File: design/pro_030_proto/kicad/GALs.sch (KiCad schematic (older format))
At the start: 11 parts, among them IC10 ATF22V10C, IC11 ATF22V10C, IC12 ATF22V10C, IC9 ATF22V10C

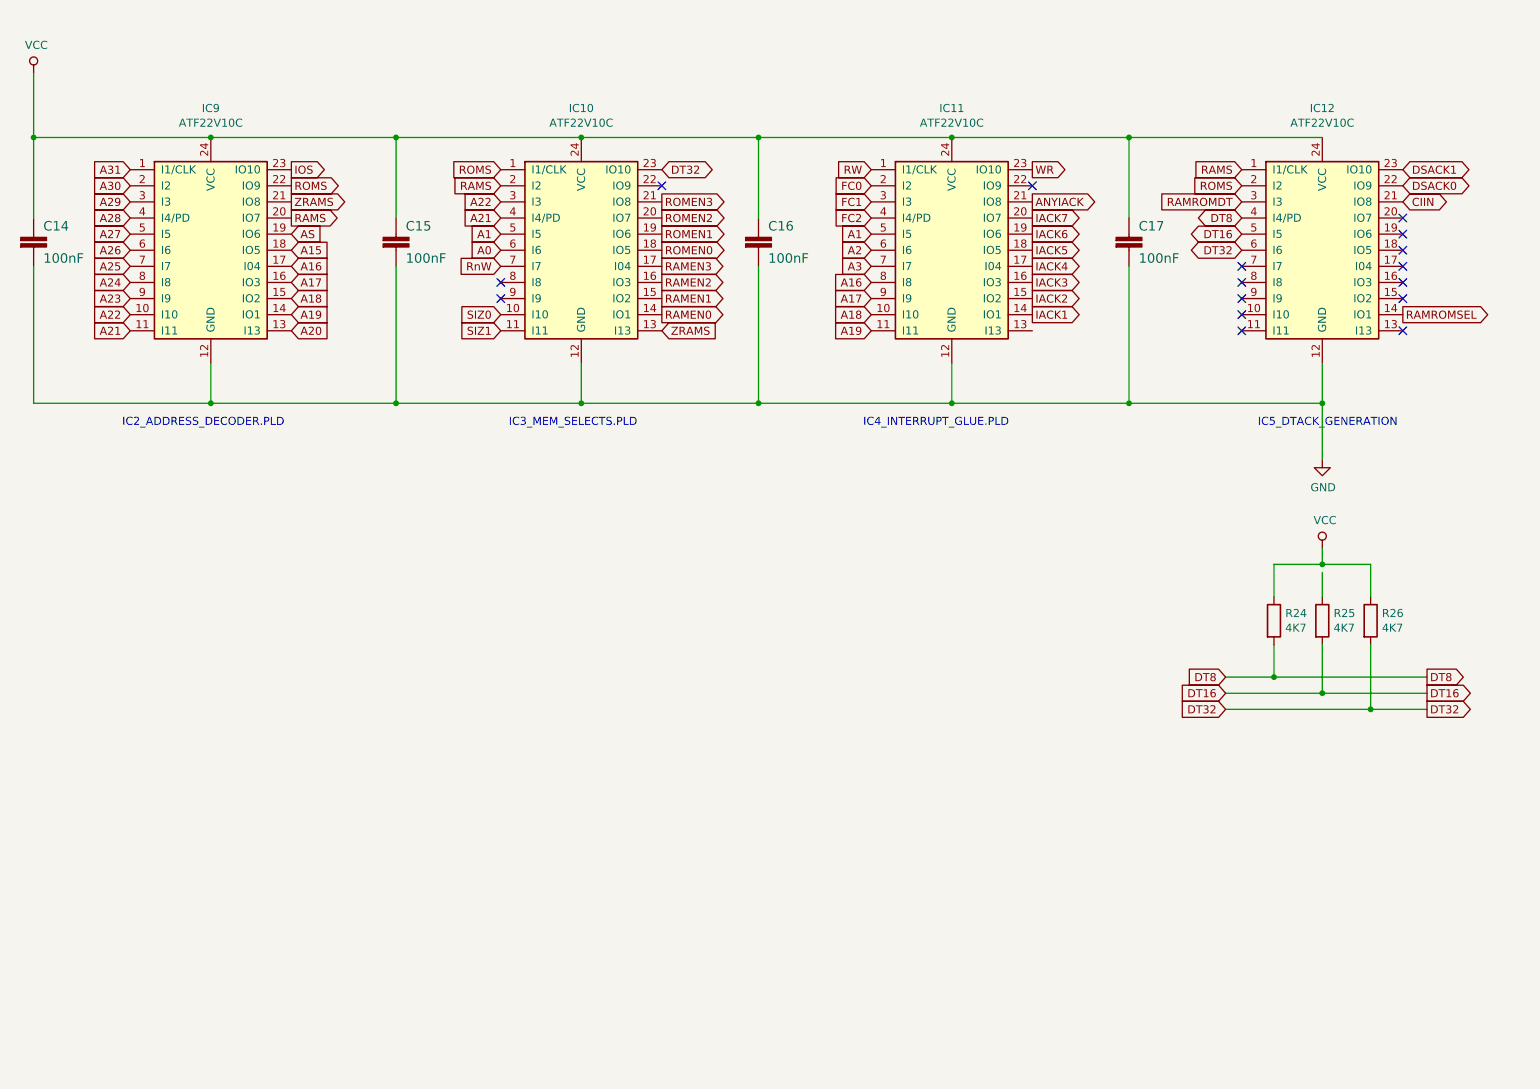
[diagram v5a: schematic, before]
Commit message: Add IO and XVID glue etc.
* Add IO Select glue
* Add Xosera glue
* Add new glues to schematic
* Clean up libs
* Reannotate (again)
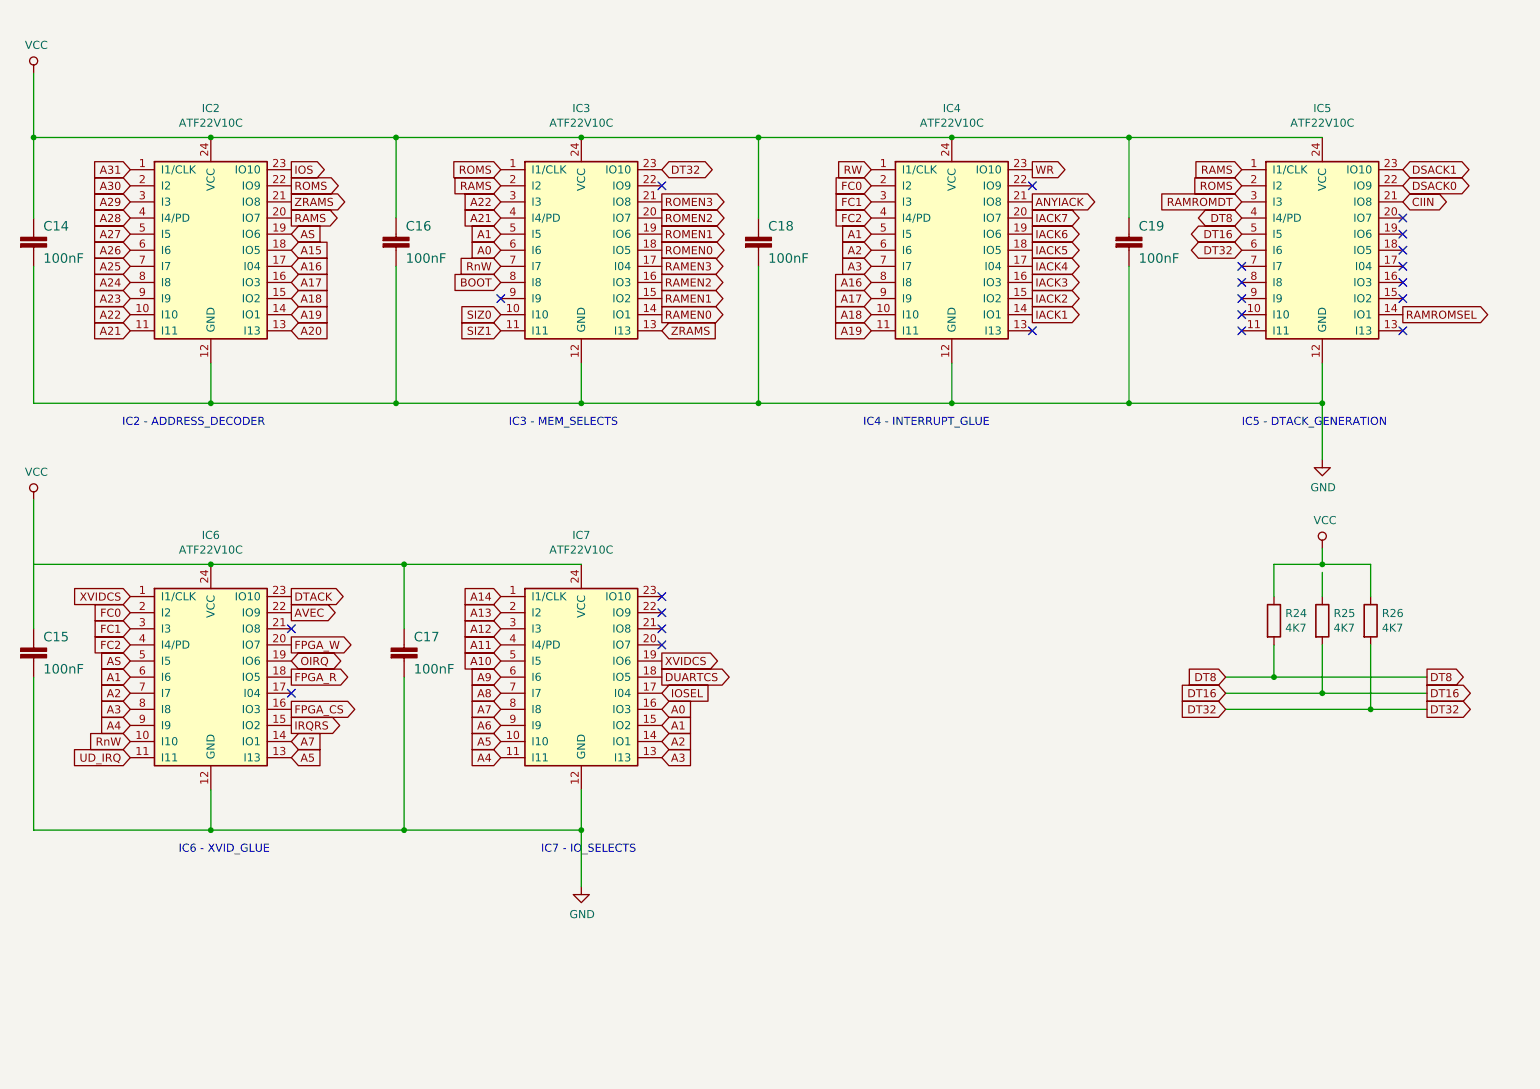
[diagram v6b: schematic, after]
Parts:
- added C15, C17: 100nF, Capacitor_THT:C_Rect_L4.0mm_W2.5mm_P2.50mm, symbol rosco_m68k-eagle-import:C2,5-3
- added IC6, IC7: ATF22V10C, Package_DIP:DIP-24_W7.62mm_Socket_LongPads, symbol rosco_m68k:GAL22V10
- renumbered C15 to C16, C16 to C18, C17 to C19, IC9 to IC2, IC10 to IC3, IC11 to IC4, IC12 to IC5
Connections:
- net labels added: A10, A11, A12, A13, A14, A4, A5, A6, A7, A8, A9, AVEC, BOOT, DTACK, DUARTCS, FPGA_CS, FPGA_R, FPGA_W, IOSEL, IRQRS, OIRQ, UD_IRQ, XVIDCS
- wire segments 43 -> 56
- no-connect marks 16 -> 22
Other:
- note added: "IC2 - ADDRESS_DECODER"
- note added: "IC3 - MEM_SELECTS"
- note added: "IC4 - INTERRUPT_GLUE"
- note added: "IC5 - DTACK_GENERATION"
- note added: "IC6 - XVID_GLUE"
- note added: "IC7 - IO_SELECTS"
- note removed: "IC2_ADDRESS_DECODER.PLD"
- note removed: "IC3_MEM_SELECTS.PLD"
- note removed: "IC4_INTERRUPT_GLUE.PLD"
- note removed: "IC5_DTACK_GENERATION"

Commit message: Finally fix ERC...
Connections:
- net labels removed: DTACK, IOSEL
- wire segments 56 -> 57
- no-connect marks 22 -> 29
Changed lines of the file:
@@
 	4700 2950 4700 3200
-$Comp
-L power:GND #PWR032
-U 1 1 60F311F4
-P 9300 3550
-F 0 "#PWR032" H 9300 3300 50  0001 C CNN
-F 1 "GND" H 9305 3377 50  0000 C CNN
-F 2 "" H 9300 3550 50  0001 C CNN
-F 3 "" H 9300 3550 50  0001 C CNN
-	1    9300 3550
-	1    0    0    -1
-$EndComp
 $Comp
 L power:VCC #PWR029
@@
 Text GLabel 6500 1750 0    50   Input ~ 0
 RW
-Wire Wire Line
-	7000 3200 7000 2950
 $Comp
 L rosco_m68k:GAL22V10 IC4
@@
 	5800 1550 7000 1550
 Connection ~ 5800 1550
-Wire Wire Line
-	7000 3200 5800 3200
 Connection ~ 5800 3200
 Wire Wire Line
@@
 Connection ~ 7000 1550
 Connection ~ 8100 1550
-Wire Wire Line
-	7000 3200 8100 3200
-Connection ~ 7000 3200
 Connection ~ 8100 3200
 Wire Wire Line
@@
 Connection ~ 9300 4200
 Wire Wire Line
-	9300 4250 9300 4400
-Wire Wire Line
 	8700 4900 9000 4900
 Wire Wire Line
@@
 Text GLabel 1900 4400 0    50   Input ~ 0
 XVIDCS
-Text GLabel 2900 4400 2    50   Output ~ 0
-DTACK
+Text GLabel 2900 4400 2    50   3State ~ 0
+DT8
 Text GLabel 2900 4500 2    50   Output ~ 0
 AVEC
@@
 Text GLabel 1900 5300 0    50   Input ~ 0
 RnW
-Text GLabel 1900 4500 0    50   Input ~ 0
-FC0
-Text GLabel 1900 4600 0    50   Input ~ 0
-FC1
-Text GLabel 1900 4700 0    50   Input ~ 0
-FC2
 Text GLabel 1900 4800 0    50   Input ~ 0
 AS
@@
 	1    0    0    -1
 $EndComp
-Text GLabel 1900 4900 0    50   Input ~ 0
-A1
-Text GLabel 1900 5000 0    50   Input ~ 0
-A2
-Text GLabel 1900 5100 0    50   Input ~ 0
-A3
-Text GLabel 1900 5200 0    50   Input ~ 0
-A4
-Text GLabel 2900 5400 2    50   Input ~ 0
-A5
-Text GLabel 2900 5300 2    50   Input ~ 0
-A7
 Text GLabel 2900 5200 2    50   Output ~ 0
 IRQRS
@@
 	1    0    0    -1
 $EndComp
-Wire Wire Line
-	1300 3800 1300 4600
-Wire Wire Line
-	2400 4200 3600 4200
 $Comp
 L rosco_m68k-eagle-import:C2,5-3 C?
@@
 	1    0    0    -1
 $EndComp
-Wire Wire Line
-	3600 4600 3600 4200
-Connection ~ 3600 4200
-Wire Wire Line
-	3600 4200 4700 4200
 Wire Wire Line
 	3600 4900 3600 5850
@@
 A0
 Text GLabel 5200 5000 2    50   Input ~ 0
-IOSEL
+IOS
 Text GLabel 5200 4900 2    50   Output ~ 0
 DUARTCS
@@
 NoConn ~ 5200 4500
 NoConn ~ 5200 4400
-NoConn ~ 7500 2750
 Text GLabel 4200 2450 0    50   Input ~ 0
 BOOT
+Wire Wire Line
+	9300 4200 9300 4400
+Wire Wire Line
+	2400 4200 3600 4200
+Wire Wire Line
+	3600 4600 3600 4200
+Connection ~ 3600 4200
+Wire Wire Line
+	3600 4200 4700 4200
+Wire Wire Line
+	1300 3800 1300 4200
+Wire Wire Line
+	1300 4200 1300 4600
+Connection ~ 1300 4200
+Text GLabel 7500 2750 2    50   Input ~ 0
+AS
+Text GLabel 1900 4500 0    50   Input ~ 0
+IACK2
+NoConn ~ 1900 4600
+NoConn ~ 1900 4700
+NoConn ~ 1900 4900
+NoConn ~ 1900 5000
+NoConn ~ 1900 5100
+NoConn ~ 1900 5200
+NoConn ~ 2900 5300
+NoConn ~ 2900 5400
+Wire Wire Line
+	5800 3200 7000 3200
+Wire Wire Line
+	7000 2950 7000 3200
+Connection ~ 7000 3200
+Wire Wire Line
+	7000 3200 8100 3200
+$Comp
+L power:GND #PWR0102
+U 1 1 616CEF14
+P 9300 3550
+F 0 "#PWR0102" H 9300 3300 50  0001 C CNN
+F 1 "GND" H 9305 3377 50  0000 C CNN
+F 2 "" H 9300 3550 50  0001 C CNN
+F 3 "" H 9300 3550 50  0001 C CNN
+	1    9300 3550
+	1    0    0    -1
+$EndComp
 $EndSCHEMATC

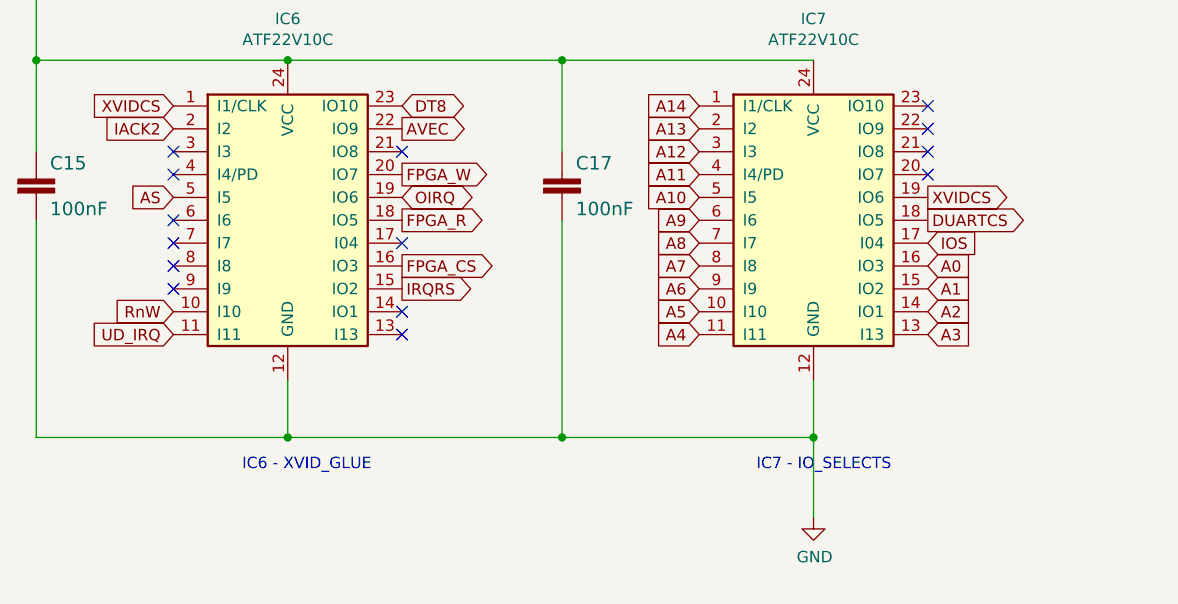
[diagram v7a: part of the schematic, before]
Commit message: Lots of work
* Sort out power and reset circuits, add ATX
* Add PCF8584 and supporting GAL code
* Stub out ATX board outline in PCB
* Various other tidying up and prep for layout
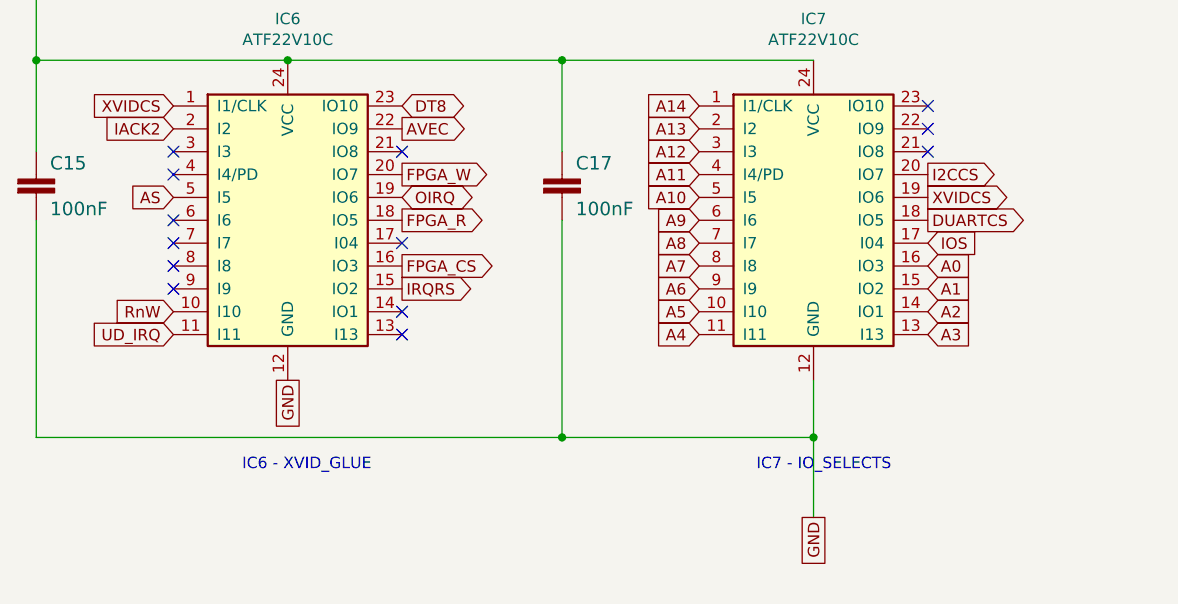
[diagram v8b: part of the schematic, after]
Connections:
- net I2CCS: now reaches IC7.20 (IO7)
- no-connect marks 29 -> 28
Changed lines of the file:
@@
 $Descr A4 11693 8268
 encoding utf-8
-Sheet 7 13
+Sheet 7 15
 Title "rosco_m68k Pro (030) Prototype"
-Date "2021-07-24"
+Date "2021-10-01"
 Rev "0"
 Comp "The Really Old-School Company Limited"
@@
 	1300 4200 2400 4200
 Connection ~ 2400 4200
-$Comp
-L power:GND #PWR031
-U 1 1 6159D82C
-P 4700 6200
-F 0 "#PWR031" H 4700 5950 50  0001 C CNN
-F 1 "GND" H 4705 6027 50  0000 C CNN
-F 2 "" H 4700 6200 50  0001 C CNN
-F 3 "" H 4700 6200 50  0001 C CNN
-	1    4700 6200
-	1    0    0    -1
-$EndComp
 Text Notes 4450 6000 0    50   ~ 0
 IC7 - IO_SELECTS
 Wire Wire Line
-	4700 6200 4700 5850
-Wire Wire Line
 	4700 5600 4700 5850
-Connection ~ 4700 5850
-Wire Wire Line
-	2400 5600 2400 5850
-Wire Wire Line
-	2400 5850 3600 5850
 $Comp
 L rosco_m68k-eagle-import:C2,5-3 C?
@@
 Wire Wire Line
 	1300 4900 1300 5850
-Wire Wire Line
-	1300 5850 2400 5850
-Connection ~ 2400 5850
 Text Notes 2200 6000 0    50   ~ 0
 IC6 - XVID_GLUE
@@
 Text GLabel 5200 4800 2    50   Output ~ 0
 XVIDCS
-NoConn ~ 5200 4700
 NoConn ~ 5200 4600
 NoConn ~ 5200 4500
@@
 	1    0    0    -1
 $EndComp
+Wire Wire Line
+	4700 5850 4700 6200
+Connection ~ 4700 5850
+Text GLabel 4700 6200 3    50   UnSpc ~ 0
+GND
+Wire Wire Line
+	1300 5850 3600 5850
+Text GLabel 2400 5600 3    50   UnSpc ~ 0
+GND
+Text GLabel 5200 4700 2    50   Output ~ 0
+I2CCS
 $EndSCHEMATC
